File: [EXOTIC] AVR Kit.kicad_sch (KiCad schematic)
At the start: 20 parts, among them J2 AVR-ISP-10, J3 USB_B, J4 Port A, J5 Port B, J6 Port C + D7, J7 Port D, SW1 SW_Push, U1 ATmega32A-P, U6 CH340C, Y1 16 MHz

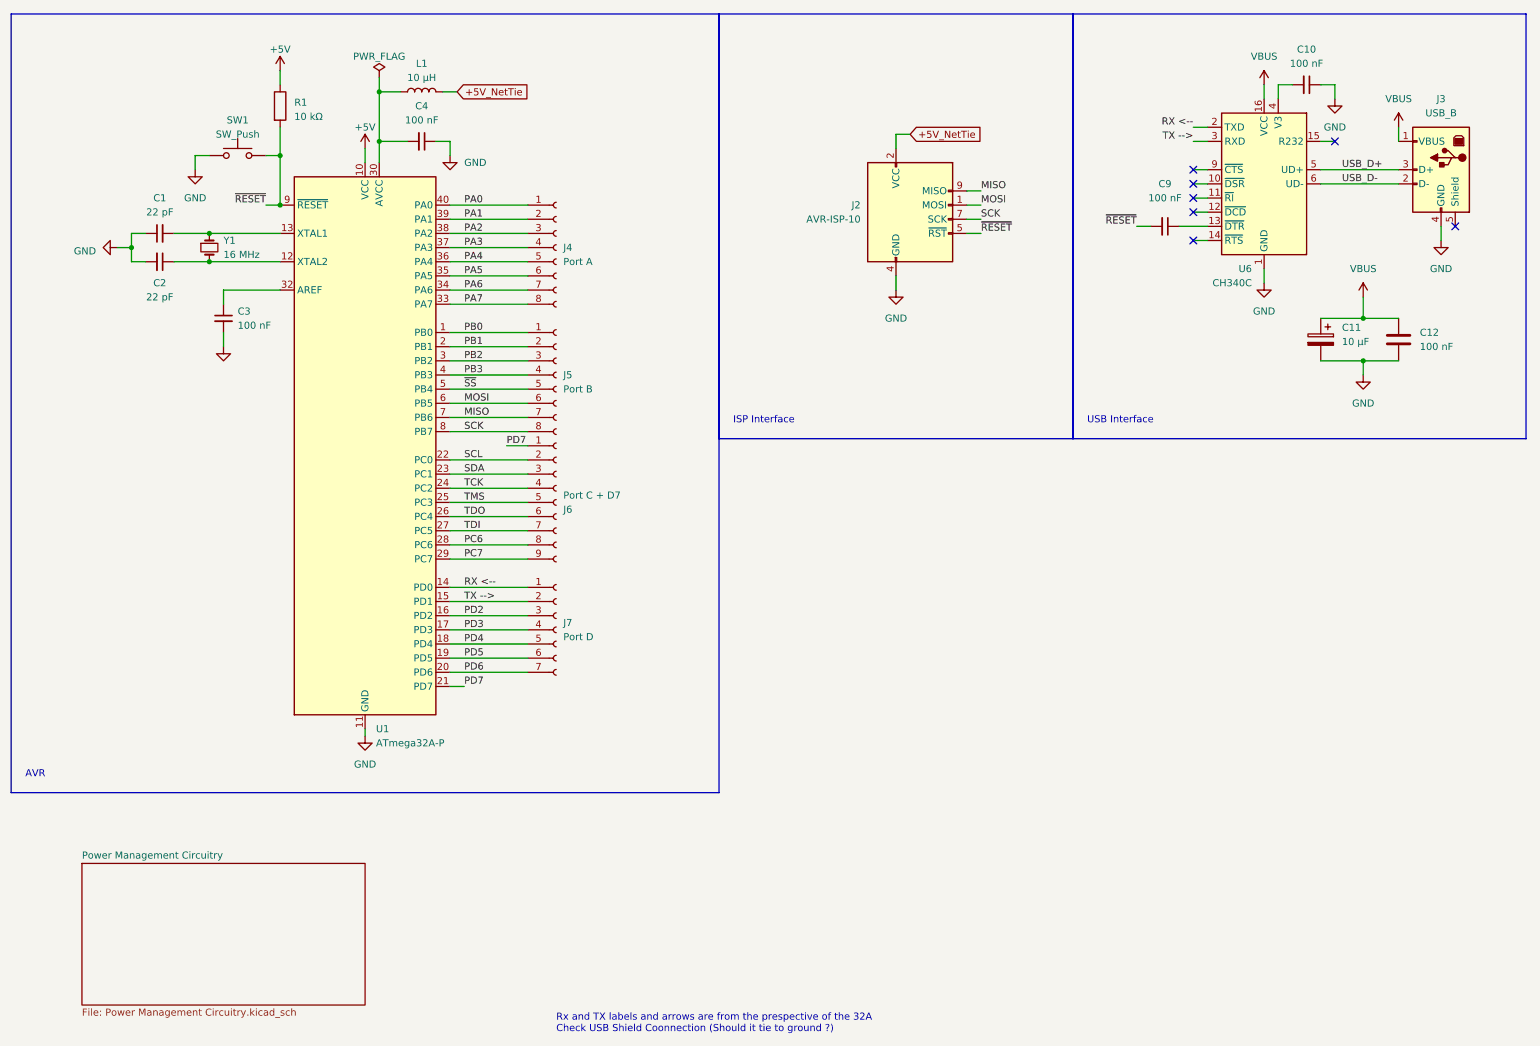
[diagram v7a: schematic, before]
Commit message: Improved Schematics' Readability
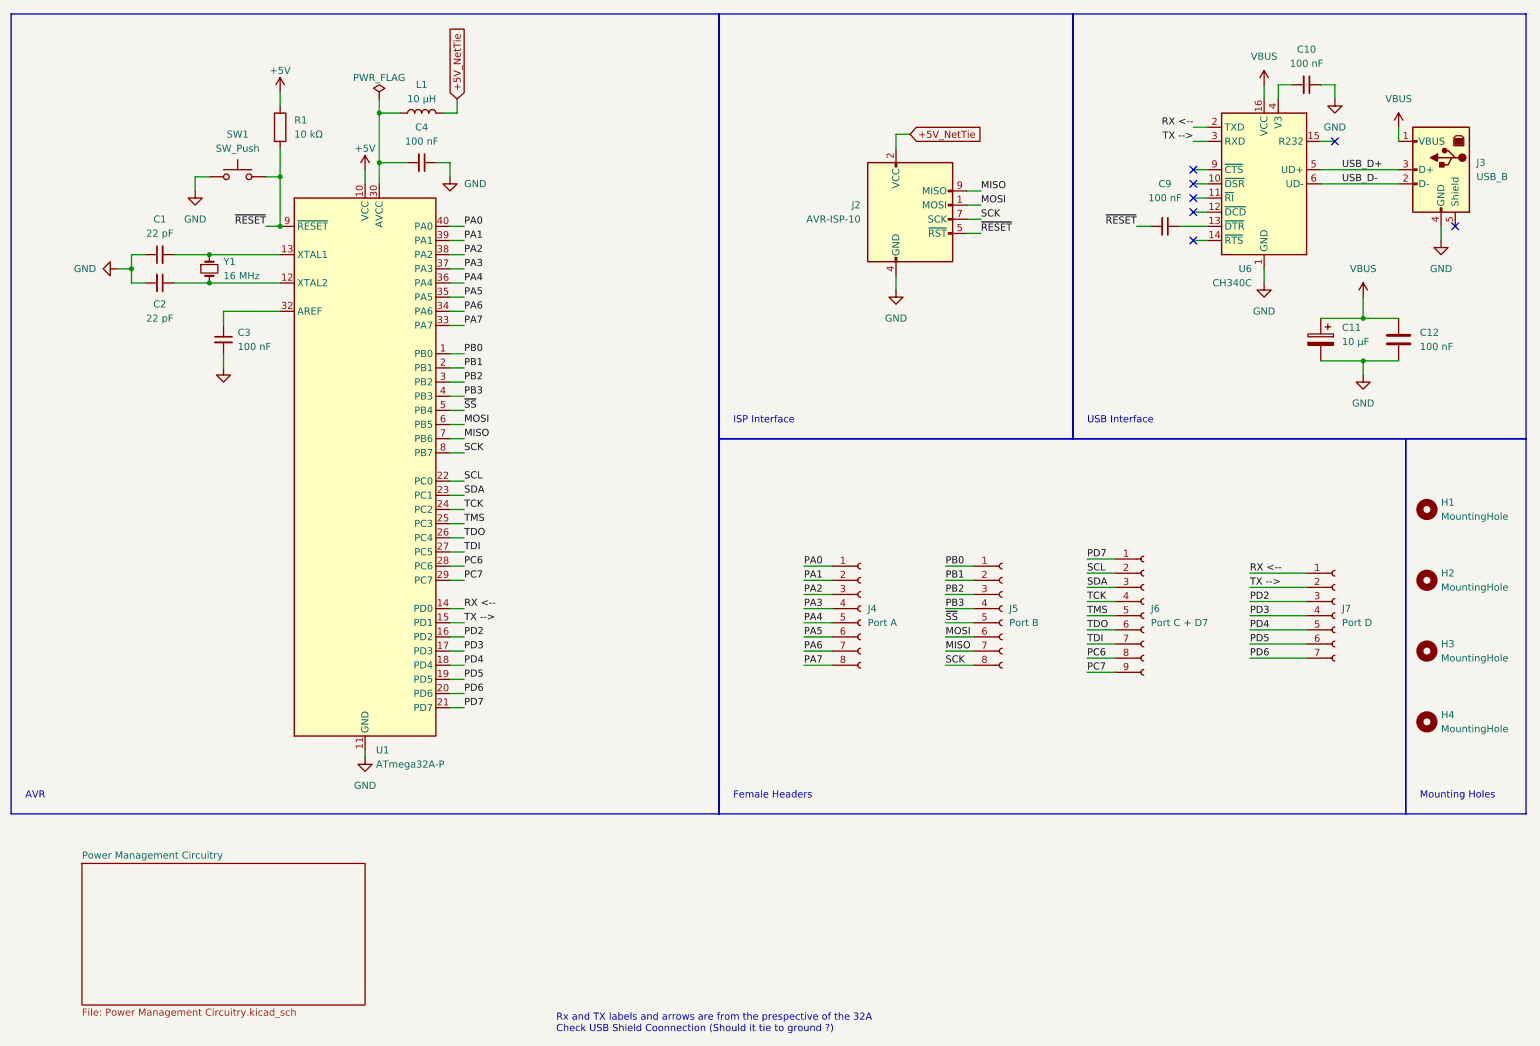
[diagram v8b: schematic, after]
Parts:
- added H1, H2, H3, H4: MountingHole, MountingHole:MountingHole_2.2mm_M2_Pad_Via, symbol Mechanical:MountingHole
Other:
- note added: "Female Headers"
- note added: "Mounting Holes"
- moved on the sheet: C1, C2, C3, C4, L1, R1, SW1, U1, Y1
